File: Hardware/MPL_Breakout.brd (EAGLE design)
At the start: 11.6 x 11.6 mm, 9 parts

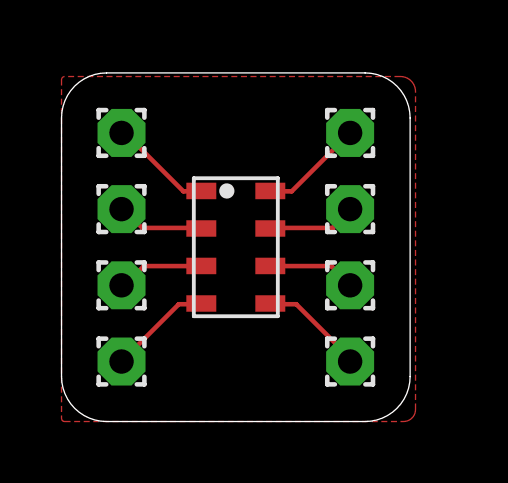
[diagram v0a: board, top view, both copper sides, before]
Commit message: updated pinheaders and names
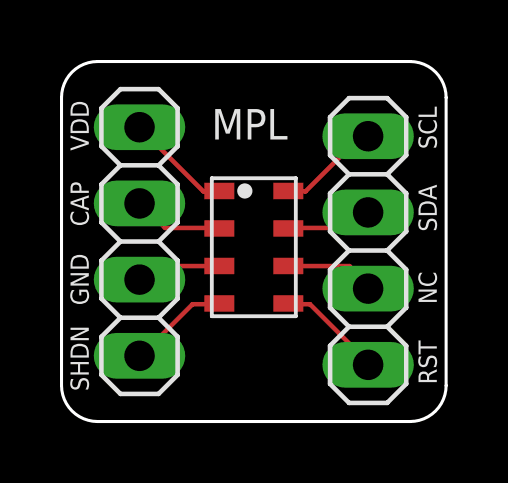
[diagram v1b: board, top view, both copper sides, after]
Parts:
- removed PAD1, PAD2, PAD3, PAD4, PAD5, PAD6, PAD7, PAD8: (no value), wirepad:1,6/0,8
- added JP1, JP2: (no value), pinhead:1X04
- moved B1 0.60 mm to (6.41, 5.81)
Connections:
- net N$1: now also JP1.4; no longer PAD1.1
- net N$2: now also JP1.3; no longer PAD2.1
- net N$3: now also JP1.2; no longer PAD3.1
- net N$4: now also JP1.1; no longer PAD4.1
- net N$5: now also JP2.4; no longer PAD5.1
- net N$6: now also JP2.3; no longer PAD6.1
- net N$7: now also JP2.2; no longer PAD7.1
- net N$8: now also JP2.1; no longer PAD8.1
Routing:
- removed copper zone on layer 1, net GND
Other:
- board size 11.6 x 11.6 mm -> 12.8 x 12 mm
- board text added: "CAP"
- board text added: "GND"
- board text added: "MPL"
- board text added: "NC"
- board text added: "RST"
- board text added: "SCL"
- board text added: "SDA"
- board text added: "SHDN"
- board text added: "VDD"
